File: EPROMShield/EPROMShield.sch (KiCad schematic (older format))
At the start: 13 parts, among them P1 Digital, P10 CONN_01X01, P11 CONN_01X01, P12 CONN_01X01, P13 CONN_01X01, P2 Power, P3 Analog, P4 Analog, P5 PWM, P6 PWM, P7 Communication, P8 CONN_01X01, P9 CONN_01X01

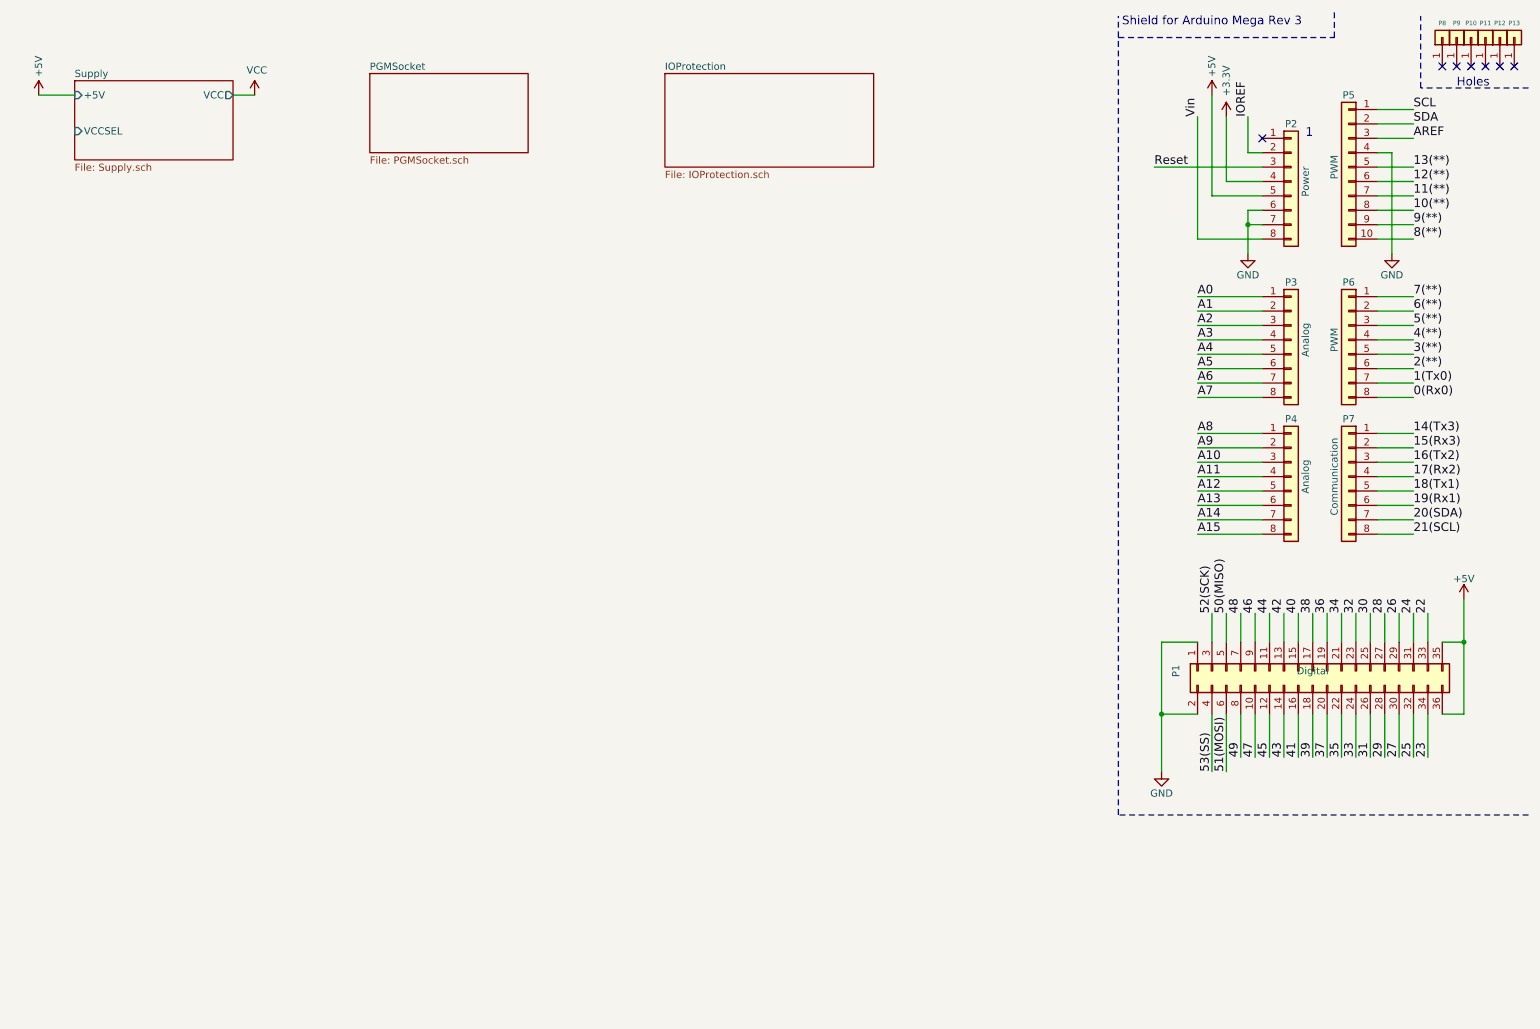
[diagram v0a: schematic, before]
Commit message: Finished schematic added caluclation for boost converter
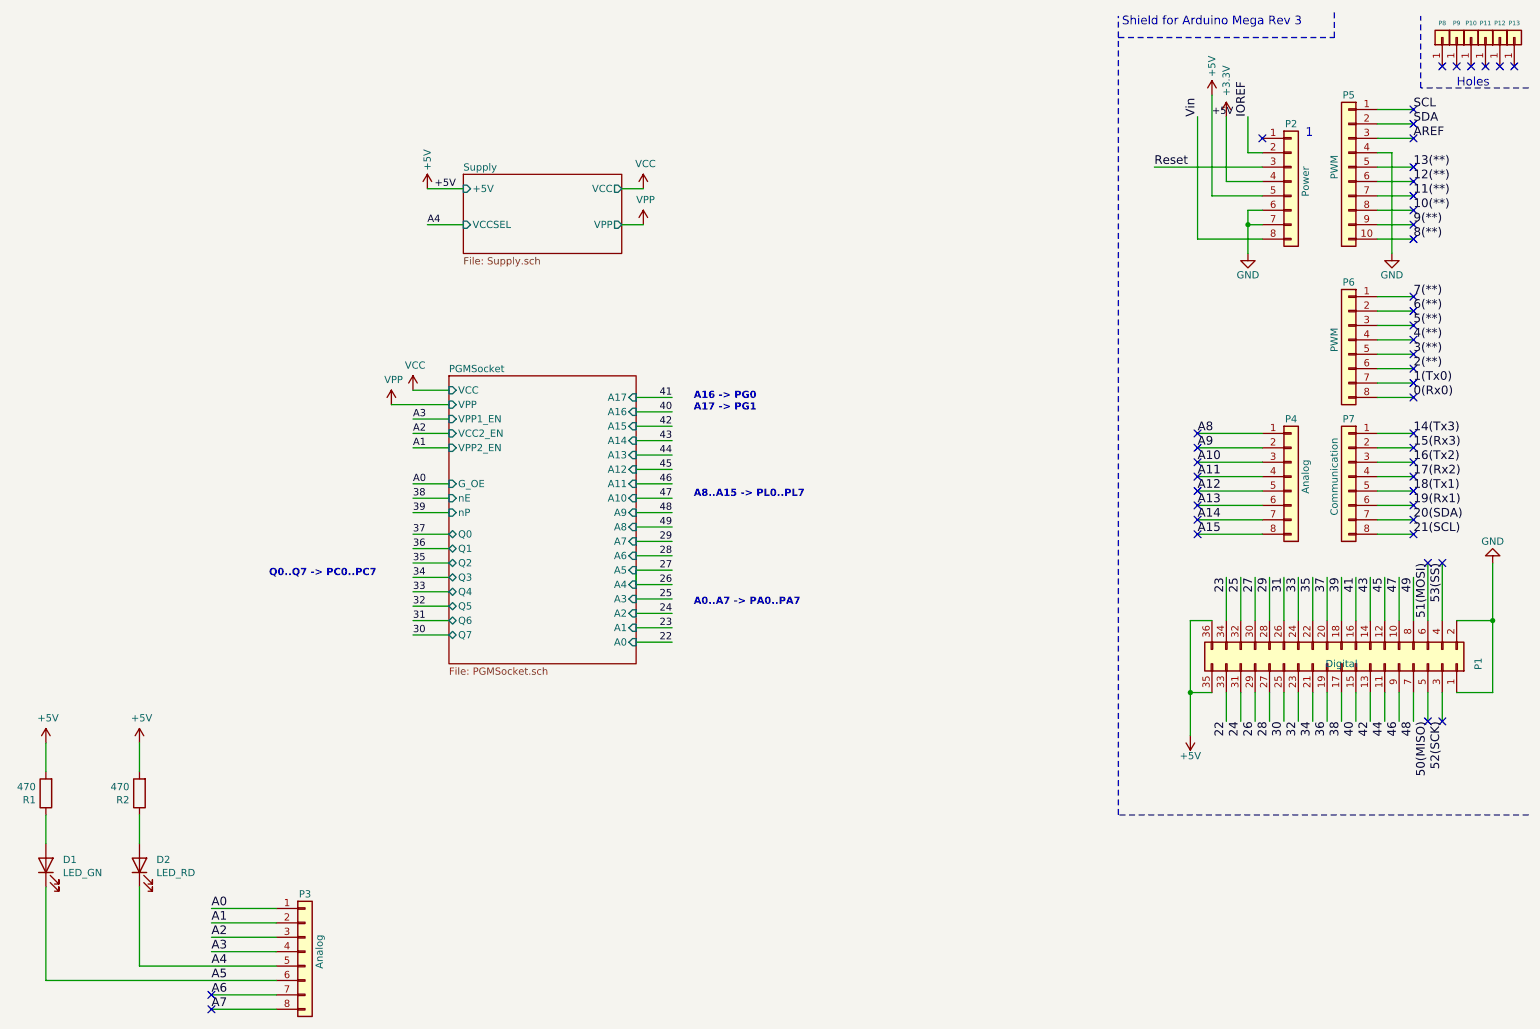
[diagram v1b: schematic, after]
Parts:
- added D1: LED_GN, symbol Device:LED
- added D2: LED_RD, symbol Device:LED
- added R1, R2: 470, symbol Device:R
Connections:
- net 27 is gone; now on net 26: P1.30 (Pin_30)
- net +5V: now also R1.2, R2.2
- net A4: now also D2.1 (K)
- net A5: now also D1.1 (K)
- new net: D1.2 (A), R1.1
- new net: D2.2 (A), R2.1
- no-connect marks 7 -> 46
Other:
- note added: "A0..A7 -> PA0..PA7"
- note added: "A16 -> PG0\nA17 -> PG1"
- note added: "A8..A15 -> PL0..PL7"
- note added: "Q0..Q7 -> PC0..PC7"
- moved on the sheet: P1, P3

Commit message: Footprints associated
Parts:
- D1, D2: footprint (none) -> LED_SMD:LED_1206_3216Metric_Pad1.42x1.75mm_HandSolder
- R1, R2: footprint (none) -> Resistor_SMD:R_0805_2012Metric_Pad1.20x1.40mm_HandSolder
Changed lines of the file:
@@
 F 0 "D1" V 939 6282 50  0000 R CNN
 F 1 "LED_GN" V 848 6282 50  0000 R CNN
-F 2 "" H 900 6400 50  0001 C CNN
+F 2 "LED_SMD:LED_1206_3216Metric_Pad1.42x1.75mm_HandSolder" H 900 6400 50  0001 C CNN
 F 3 "~" H 900 6400 50  0001 C CNN
 	1    900  6400
@@
 F 0 "R1" H 970 5946 50  0000 L CNN
 F 1 "470" H 970 5855 50  0000 L CNN
-F 2 "" V 830 5900 50  0001 C CNN
+F 2 "Resistor_SMD:R_0805_2012Metric_Pad1.20x1.40mm_HandSolder" V 830 5900 50  0001 C CNN
 F 3 "~" H 900 5900 50  0001 C CNN
 	1    900  5900
@@
 F 0 "D2" V 1589 6282 50  0000 R CNN
 F 1 "LED_RD" V 1498 6282 50  0000 R CNN
-F 2 "" H 1550 6400 50  0001 C CNN
+F 2 "LED_SMD:LED_1206_3216Metric_Pad1.42x1.75mm_HandSolder" H 1550 6400 50  0001 C CNN
 F 3 "~" H 1550 6400 50  0001 C CNN
 	1    1550 6400
@@
 F 0 "R2" H 1620 5946 50  0000 L CNN
 F 1 "470" H 1620 5855 50  0000 L CNN
-F 2 "" V 1480 5900 50  0001 C CNN
+F 2 "Resistor_SMD:R_0805_2012Metric_Pad1.20x1.40mm_HandSolder" V 1480 5900 50  0001 C CNN
 F 3 "~" H 1550 5900 50  0001 C CNN
 	1    1550 5900

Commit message: First Version routing is done
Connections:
- net 26: no longer P1.30 (Pin_30)
- new net 27: P1.30 (Pin_30)
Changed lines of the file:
@@
 Wire Wire Line
 	4900 1700 5050 1700
-$Sheet
-S 3700 3000 1300 2000
-U 6126FB03
-F0 "PGMSocket" 50
-F1 "PGMSocket.sch" 50
-F2 "VCC" I L 3700 3100 50
-F3 "VPP" I L 3700 3200 50
-F4 "VPP1_EN" I L 3700 3300 50
-F5 "VCC2_EN" I L 3700 3400 50
-F6 "A17" I R 5000 3150 50
-F7 "VPP2_EN" I L 3700 3500 50
-F8 "G_OE" I L 3700 3750 50
-F9 "A16" I R 5000 3250 50
-F10 "A15" I R 5000 3350 50
-F11 "A12" I R 5000 3650 50
-F12 "A7" I R 5000 4150 50
-F13 "A6" I R 5000 4250 50
-F14 "A5" I R 5000 4350 50
-F15 "A4" I R 5000 4450 50
-F16 "A3" I R 5000 4550 50
-F17 "A2" I R 5000 4650 50
-F18 "A1" I R 5000 4750 50
-F19 "A0" I R 5000 4850 50
-F20 "nE" I L 3700 3850 50
-F21 "A11" I R 5000 3750 50
-F22 "A9" I R 5000 3950 50
-F23 "A8" I R 5000 4050 50
-F24 "A13" I R 5000 3550 50
-F25 "A14" I R 5000 3450 50
-F26 "nP" I L 3700 3950 50
-F27 "Q0" B L 3700 4100 50
-F28 "Q1" B L 3700 4200 50
-F29 "Q2" B L 3700 4300 50
-F30 "Q3" B L 3700 4400 50
-F31 "Q4" B L 3700 4500 50
-F32 "Q5" B L 3700 4600 50
-F33 "Q6" B L 3700 4700 50
-F34 "Q7" B L 3700 4800 50
-F35 "A10" I R 5000 3850 50
-$EndSheet
 Wire Wire Line
 	3700 4100 3450 4100
@@
 	5000 4550 5250 4550
 Wire Wire Line
-	5000 4450 5000 4350
-Wire Wire Line
-	5000 4450 5250 4450
-Wire Wire Line
-	5000 4350 5250 4350
-Wire Wire Line
 	5000 4250 5250 4250
 Wire Wire Line
@@
 Text Label 5250 4550 2    50   ~ 0
 25
-Text Label 5250 4450 2    50   ~ 0
-26
-Text Label 5250 4350 2    50   ~ 0
-27
 Text Label 5250 4250 2    50   ~ 0
 28
@@
 	1    0    0    -1
 $EndComp
-Wire Wire Line
-	900  5550 900  5750
 $Comp
 L Device:LED D?
@@
 Text Label 3600 1700 0    50   ~ 0
 +5V
+Wire Wire Line
+	5000 4350 5250 4350
+Wire Wire Line
+	5000 4450 5250 4450
+$Sheet
+S 3700 3000 1300 2000
+U 6126FB03
+F0 "PGMSocket" 50
+F1 "PGMSocket.sch" 50
+F2 "VCC" I L 3700 3100 50
+F3 "VPP" I L 3700 3200 50
+F4 "VPP1_EN" I L 3700 3300 50
+F5 "VCC2_EN" I L 3700 3400 50
+F6 "A17" I R 5000 3150 50
+F7 "VPP2_EN" I L 3700 3500 50
+F8 "G_OE" I L 3700 3750 50
+F9 "A16" I R 5000 3250 50
+F10 "A15" I R 5000 3350 50
+F11 "A12" I R 5000 3650 50
+F12 "A7" I R 5000 4150 50
+F13 "A6" I R 5000 4250 50
+F14 "A5" I R 5000 4350 50
+F15 "A4" I R 5000 4450 50
+F16 "A3" I R 5000 4550 50
+F17 "A2" I R 5000 4650 50
+F18 "A1" I R 5000 4750 50
+F19 "A0" I R 5000 4850 50
+F20 "nE" I L 3700 3850 50
+F21 "A11" I R 5000 3750 50
+F22 "A9" I R 5000 3950 50
+F23 "A8" I R 5000 4050 50
+F24 "A13" I R 5000 3550 50
+F25 "A14" I R 5000 3450 50
+F26 "nP" I L 3700 3950 50
+F27 "PQ0" B L 3700 4100 50
+F28 "PQ1" B L 3700 4200 50
+F29 "PQ2" B L 3700 4300 50
+F30 "PQ3" B L 3700 4400 50
+F31 "PQ4" B L 3700 4500 50
+F32 "PQ5" B L 3700 4600 50
+F33 "PQ6" B L 3700 4700 50
+F34 "PQ7" B L 3700 4800 50
+F35 "A10" I R 5000 3850 50
+$EndSheet
+Text Label 5250 4350 2    50   ~ 0
+27
+Text Label 5250 4450 2    50   ~ 0
+26
+Wire Wire Line
+	900  5550 900  5750
 $EndSCHEMATC
